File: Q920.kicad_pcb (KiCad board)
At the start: 2 copper layers, 61.6 x 36.8 mm, 10 parts, among them J2 XH-B4B, J3 出力側 USB_A, J4 SW pin/Conn_01x02_Socket, J5 TEST POINT, U1 TLP222A

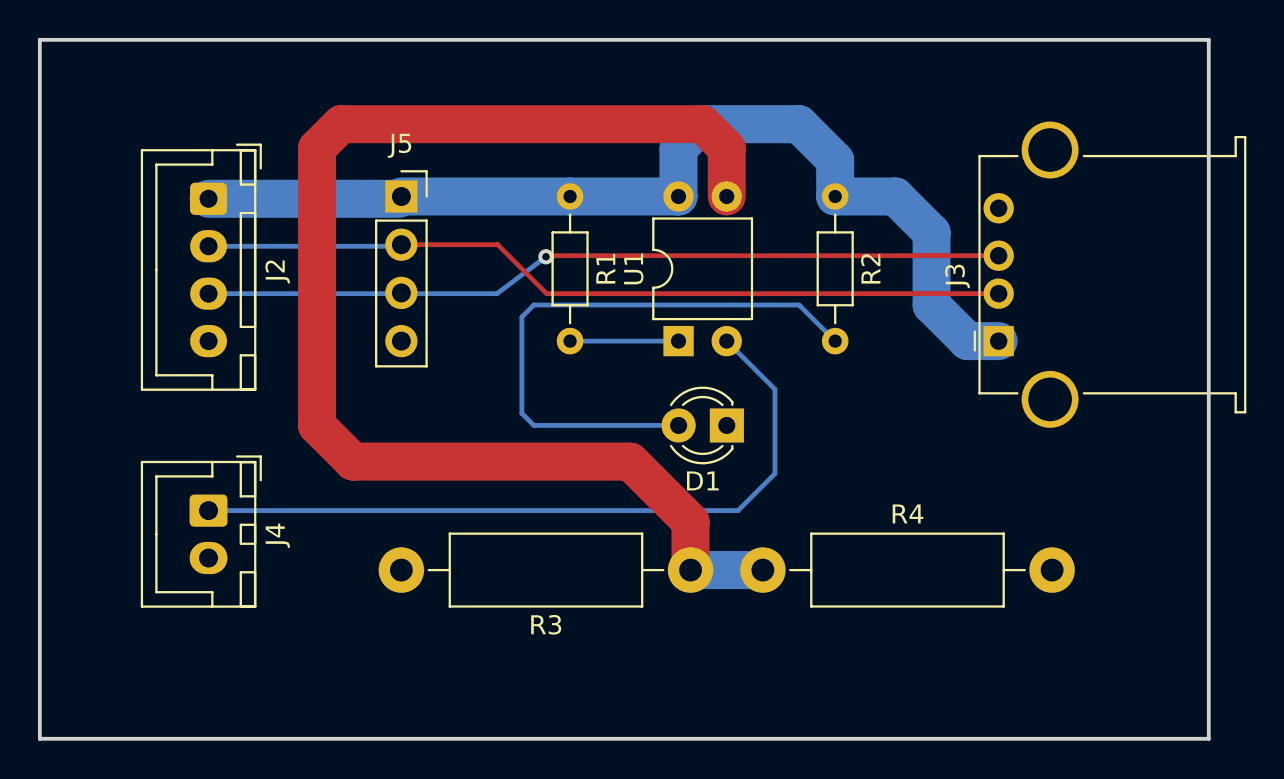
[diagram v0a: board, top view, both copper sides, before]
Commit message: cad: リレーを抵抗に変更した
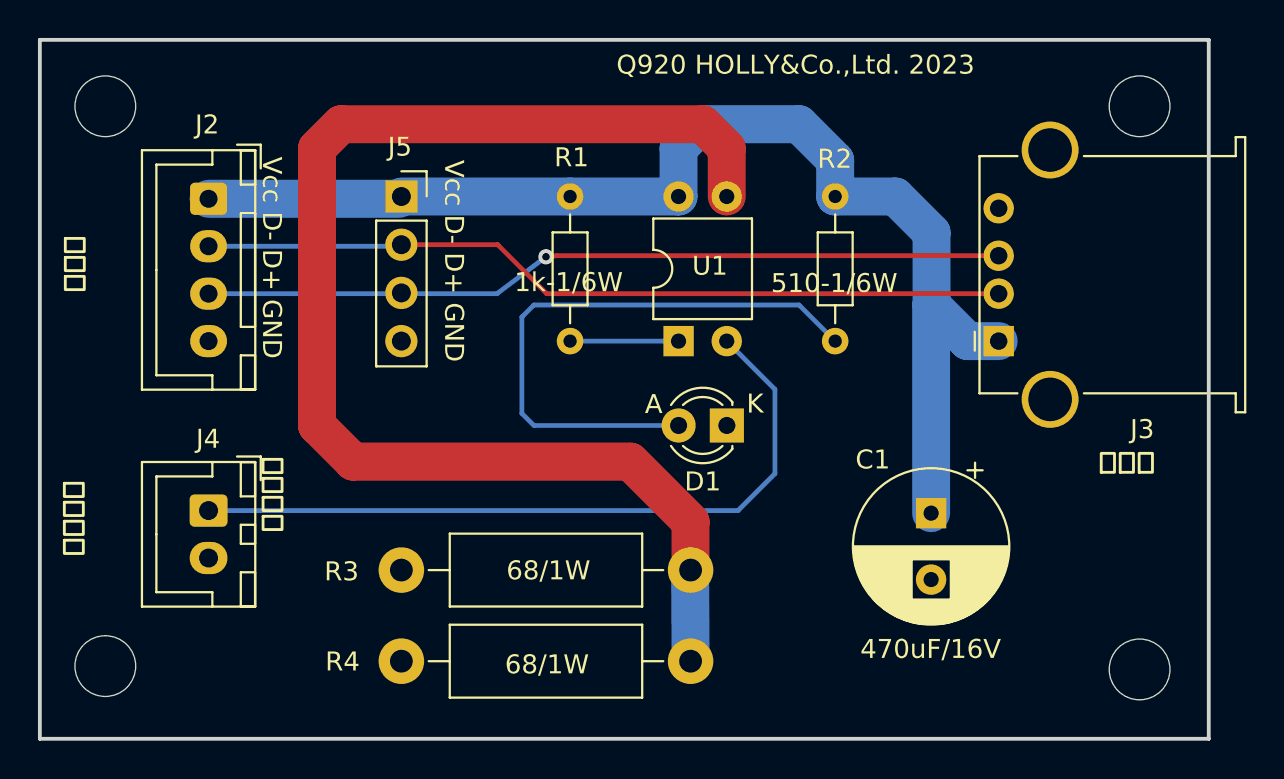
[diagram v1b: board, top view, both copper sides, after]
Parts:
- added C1: 470uF/16V, Capacitor_THT:CP_Radial_D8.0mm_P3.50mm, F.Cu at (129.5, 85.3)
- added REF**: MountingHole_3.2mm_M3, MountingHole:MountingHole_3.2mm_M3, F.Cu at (86.0, 64.0)
- added REF**: MountingHole_3.2mm_M3, MountingHole:MountingHole_3.2mm_M3, F.Cu at (140.5, 64.0)
- added REF**: MountingHole_3.2mm_M3, MountingHole:MountingHole_3.2mm_M3, F.Cu at (140.6, 93.5)
- added REF**: MountingHole_3.2mm_M3, MountingHole:MountingHole_3.2mm_M3, F.Cu at (86.0, 93.5)
- moved R4 6.13 mm to (116.8, 93.1), turned to 180 degrees
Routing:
- net /VBUS: track 52.8 -> 63.8 mm
- net Net-(R3-Pad1): track 67.9 -> 68.9 mm
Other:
- board text added: "A"
- board text added: "K"
- board text added: "Q920 HOLLY&Co.,Ltd. 2023"
- board text added: "Vcc D- D+ GND"
- board text added: "トリガー"
- board text added: "入力側"
- board text added: "出力側"

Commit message: pcb: 社名変更
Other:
- board text added: "Q920 LLC YS-Lab 2023"
- board text removed: "Q920 HOLLY&Co.,Ltd. 2023"
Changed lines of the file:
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@@
     (effects (font (size 1 1) (thickness 0.15)) (justify left bottom))
   )
-  (gr_text "Q920 HOLLY&Co.,Ltd. 2023" (at 112.9284 62.23) (layer "F.SilkS")
+  (gr_text "Q920 LLC YS-Lab 2023" (at 112.9284 62.23) (layer "F.SilkS")
     (effects (font (size 1 1) (thickness 0.15)) (justify left bottom))
   )
@@
     (effects (font (size 1 1) (thickness 0.15)) (justify left bottom))
   )
+  (gr_text "Vcc D- D+ GND" (at 131.191 78.9432 90) (layer "F.SilkS")
+    (effects (font (size 1 1) (thickness 0.15)) (justify left bottom))
+  )
